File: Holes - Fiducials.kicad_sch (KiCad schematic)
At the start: 0 parts

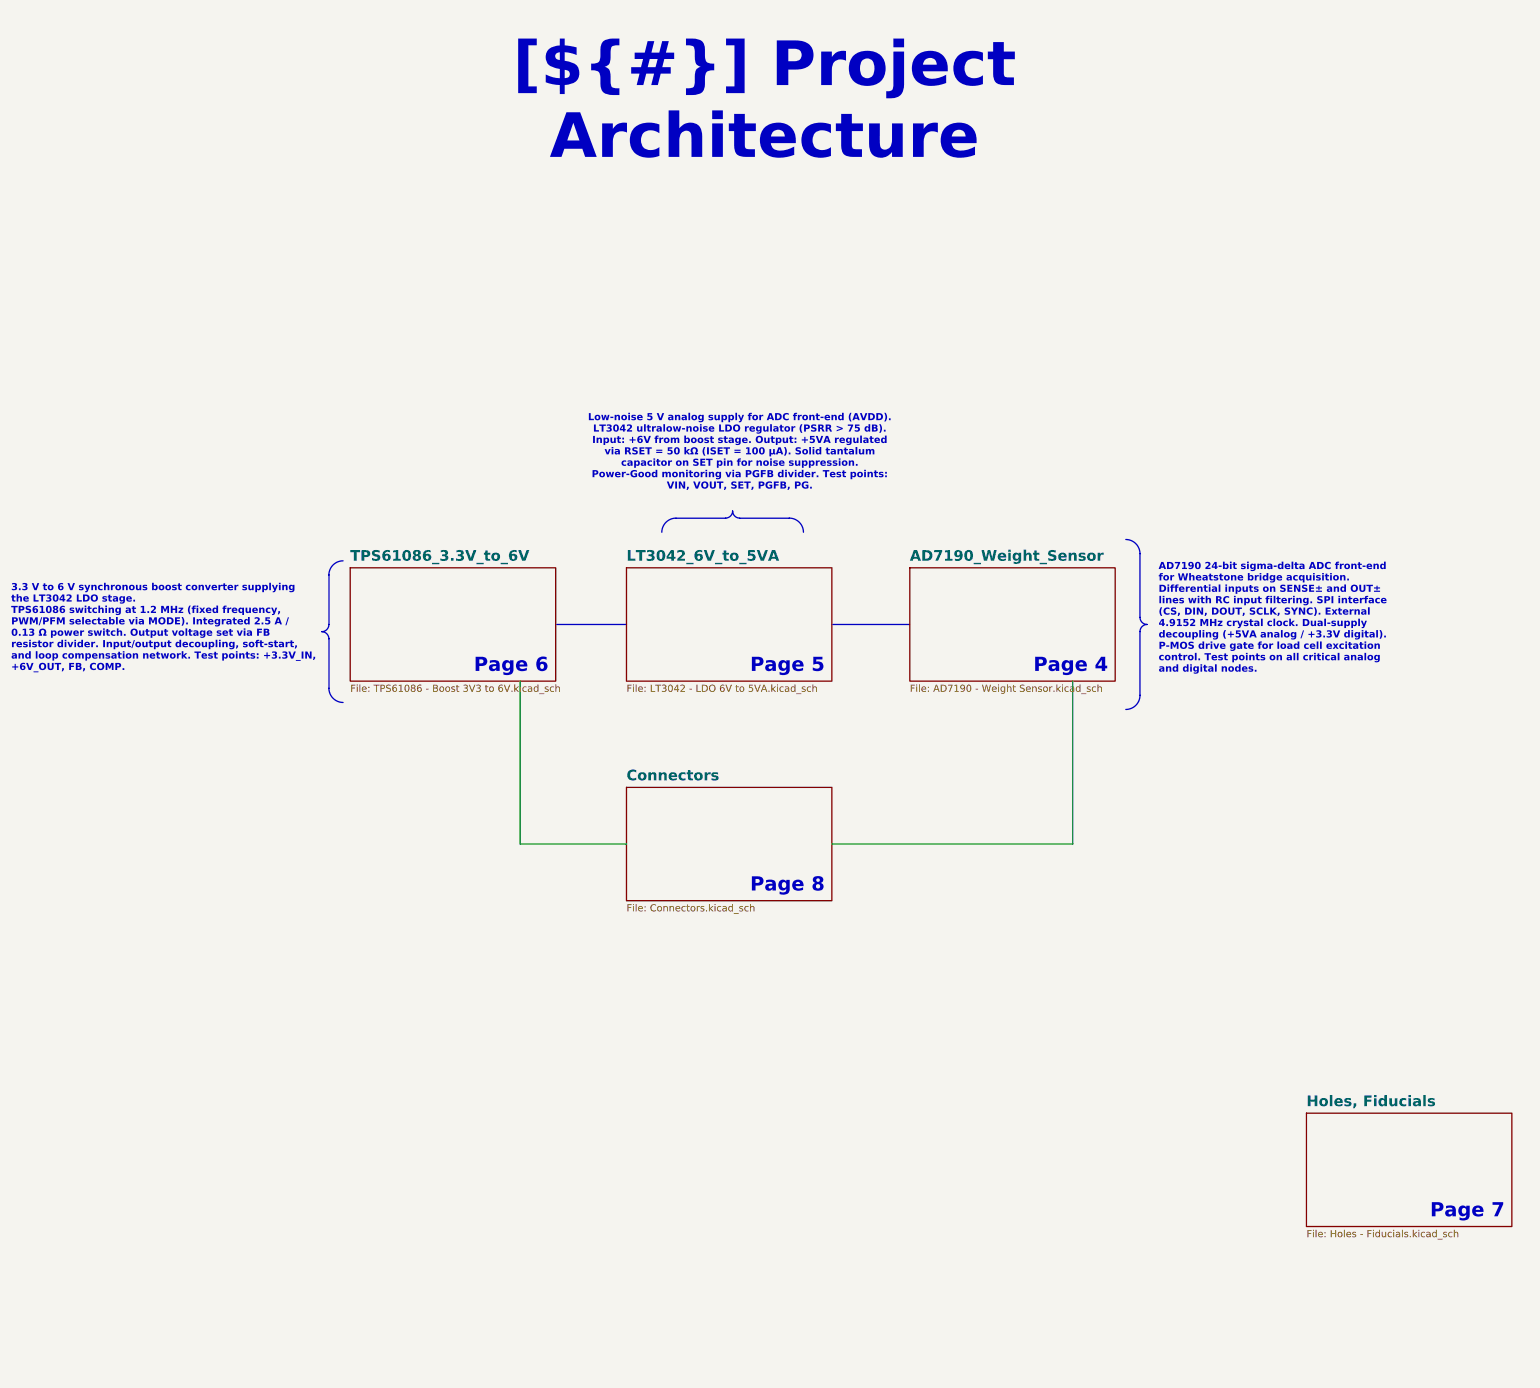
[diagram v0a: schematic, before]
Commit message: Clean up project for KDT template: rename, metadata, KiCad 10 CI
- Rename project Cellule_de_force_V2 -> OPEN_WEIGHT and sheets after their function
  (fix AD7910 -> AD7190 typo), update all sheet/project references in sch/pcb/pro
- Real title-block titles, sheet headers use ${TITLE}, restore KDT drawing sheets,
  remove template leftovers from PCB title block
- kibot_main.yaml: COMPANY = OPEN THRUST LAB, GIT_URL = foukouda/OPEN_WEIGHT
- CI: add KiCad 10 (KiBot v2_dk10), PRELIMINARY variant on dev
- README now generated from kibot_resources/templates/readme.txt; fill CHANGELOG
- Move mechanical CAD to Mechanical/, extend .gitignore, untrack 3Dx logs

Co-Authored-By: Claude Opus 5.5 <noreply@anthropic.com>
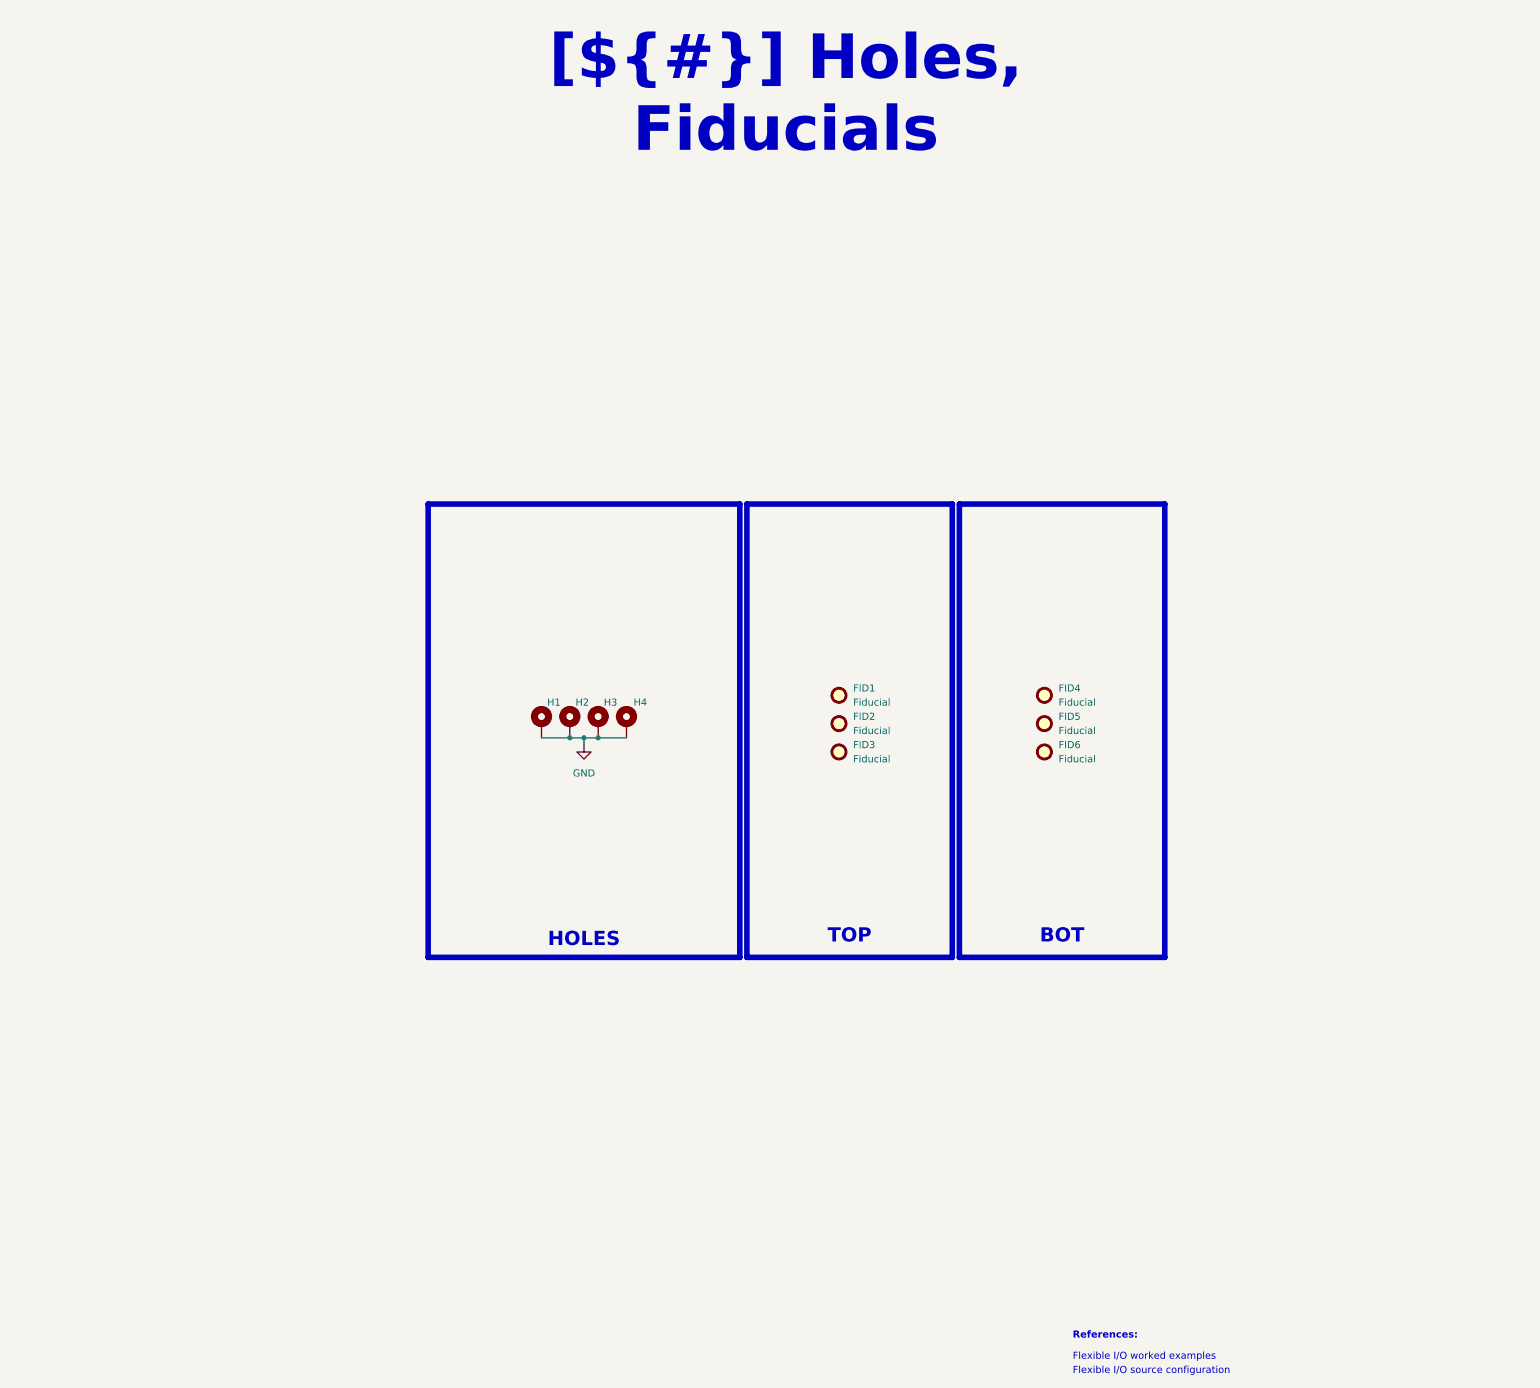
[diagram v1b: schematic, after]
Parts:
- added FID1, FID2, FID3, FID4, FID5, FID6: Fiducial, Fiducial:Fiducial_1.5mm_Mask3mm, symbol Mechanical:Fiducial
- added H1, H2, H3, H4: MountingHole_Pad, MountingHole:MountingHole_3.2mm_M3_Pad_Via, symbol Mechanical:MountingHole_Pad
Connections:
- new net GND: H1.1, H2.1, H3.1, H4.1
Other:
- removed sheet AD7190_Weight_Sensor
- removed sheet Connectors
- removed sheet Holes, Fiducials
- removed sheet LT3042_6V_to_5VA
- removed sheet TPS61086_3.3V_to_6V
- note added: "Flexible I/O source configuration"
- note added: "Flexible I/O worked examples"
- note added: "References:"
- note removed: "Page 4"
- note removed: "Page 5"
- note removed: "Page 6"
- note removed: "Page 7"
- note removed: "Page 8"
- title: Project Architecture -> Holes, Fiducials

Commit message: Self-contained libraries, JLCPCB rules, ERC/DRC cleanup
- lib/: project symbol library (19 symbols), footprint library (17 footprints)
  and all 3D models (15), referenced through ${KIPRJMOD} + project lib tables.
  A fresh clone now opens with every symbol, footprint and 3D model.
- Remove duplicated / absolute 3D model paths (C:/Users/..., ${KICAD_FOOTPRINT})
- OPEN_WEIGHT.kicad_dru: JLCPCB 4-layer rules; stackup JLC04161H-7628; board minimums
- AD7190 footprint: drop per-pad 0.102 mm mask margin (mask bridges at 0.65 mm pitch)
- Exclude unplaced TP/FID symbols from board; PWR_FLAGs; decorative wires -> lines
- Local text variables in .kicad_pro; Revision History wired to [Unreleased]
- get_changelog.py: accept "## [Unreleased]" without date
ERC: 0 errors. DRC: 0 errors except 10 courtyard overlaps (placement), 0 parity issues.

Co-Authored-By: Claude Opus 5.5 <noreply@anthropic.com>
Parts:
- FID1, FID2, FID3, FID4, FID5, FID6: symbol Mechanical:Fiducial -> OPEN_WEIGHT:Fiducial
- H1, H2, H3, H4: footprint MountingHole:MountingHole_3.2mm_M3_Pad_Via -> OPEN_WEIGHT:MountingHole_3.2mm_M3_Pad_Via; symbol Mechanical:MountingHole_Pad -> OPEN_WEIGHT:MountingHole_Pad
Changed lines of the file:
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@@
 	)
 	(symbol
-		(lib_id "Mechanical:Fiducial")
+		(lib_id "OPEN_WEIGHT:Fiducial")
 		(at 223.52 139.7 0)
 		(unit 1)
@@
 		(exclude_from_sim no)
 		(in_bom no)
-		(on_board yes)
-		(in_pos_files yes)
+		(on_board no)
+		(in_pos_files no)
 		(dnp no)
 		(fields_autoplaced yes)
@@
 	)
 	(symbol
-		(lib_id "Mechanical:MountingHole_Pad")
+		(lib_id "OPEN_WEIGHT:MountingHole_Pad")
 		(at 185.42 139.7 0)
 		(unit 1)
@@
 			)
 		)
-		(property "Footprint" "MountingHole:MountingHole_3.2mm_M3_Pad_Via"
+		(property "Footprint" "OPEN_WEIGHT:MountingHole_3.2mm_M3_Pad_Via"
 			(at 185.42 139.7 0)
 			(hide yes)
@@
 	)
 	(symbol
-		(lib_id "Mechanical:MountingHole_Pad")
+		(lib_id "OPEN_WEIGHT:MountingHole_Pad")
 		(at 170.18 139.7 0)
 		(unit 1)
@@
 			)
 		)
-		(property "Footprint" "MountingHole:MountingHole_3.2mm_M3_Pad_Via"
+		(property "Footprint" "OPEN_WEIGHT:MountingHole_3.2mm_M3_Pad_Via"
 			(at 170.18 139.7 0)
 			(hide yes)
@@
 	)
 	(symbol
-		(lib_id "Mechanical:Fiducial")
+		(lib_id "OPEN_WEIGHT:Fiducial")
 		(at 223.52 144.78 0)
 		(unit 1)
@@
 		(exclude_from_sim no)
 		(in_bom no)
-		(on_board yes)
-		(in_pos_files yes)
+		(on_board no)
+		(in_pos_files no)
 		(dnp no)
 		(fields_autoplaced yes)
@@
 	)
 	(symbol
-		(lib_id "Mechanical:MountingHole_Pad")
+		(lib_id "OPEN_WEIGHT:MountingHole_Pad")
 		(at 175.26 139.7 0)
 		(unit 1)
@@
 			)
 		)
-		(property "Footprint" "MountingHole:MountingHole_3.2mm_M3_Pad_Via"
+		(property "Footprint" "OPEN_WEIGHT:MountingHole_3.2mm_M3_Pad_Via"
 			(at 175.26 139.7 0)
 			(hide yes)
@@
 	)
 	(symbol
-		(lib_id "Mechanical:Fiducial")
+		(lib_id "OPEN_WEIGHT:Fiducial")
 		(at 260.35 134.62 0)
 		(unit 1)
@@
 		(exclude_from_sim no)
 		(in_bom no)
-		(on_board yes)
-		(in_pos_files yes)
+		(on_board no)
+		(in_pos_files no)
 		(dnp no)
 		(fields_autoplaced yes)
@@
 	)
 	(symbol
-		(lib_id "Mechanical:Fiducial")
+		(lib_id "OPEN_WEIGHT:Fiducial")
 		(at 260.35 144.78 0)
 		(unit 1)
@@
 		(exclude_from_sim no)
 		(in_bom no)
-		(on_board yes)
-		(in_pos_files yes)
+		(on_board no)
+		(in_pos_files no)
 		(dnp no)
 		(fields_autoplaced yes)
@@
 	)
 	(symbol
-		(lib_id "Mechanical:MountingHole_Pad")
+		(lib_id "OPEN_WEIGHT:MountingHole_Pad")
 		(at 180.34 139.7 0)
 		(unit 1)
@@
 			)
 		)
-		(property "Footprint" "MountingHole:MountingHole_3.2mm_M3_Pad_Via"
+		(property "Footprint" "OPEN_WEIGHT:MountingHole_3.2mm_M3_Pad_Via"
 			(at 180.34 139.7 0)
 			(hide yes)
@@
 	)
 	(symbol
-		(lib_id "Mechanical:Fiducial")
+		(lib_id "OPEN_WEIGHT:Fiducial")
 		(at 260.35 139.7 0)
 		(unit 1)
@@
 		(exclude_from_sim no)
 		(in_bom no)
-		(on_board yes)
-		(in_pos_files yes)
+		(on_board no)
+		(in_pos_files no)
 		(dnp no)
 		(fields_autoplaced yes)
@@
 	)
 	(symbol
-		(lib_id "Mechanical:Fiducial")
+		(lib_id "OPEN_WEIGHT:Fiducial")
 		(at 223.52 134.62 0)
 		(unit 1)
@@
 		(exclude_from_sim no)
 		(in_bom no)
-		(on_board yes)
-		(in_pos_files yes)
+		(on_board no)
+		(in_pos_files no)
 		(dnp no)
 		(fields_autoplaced yes)

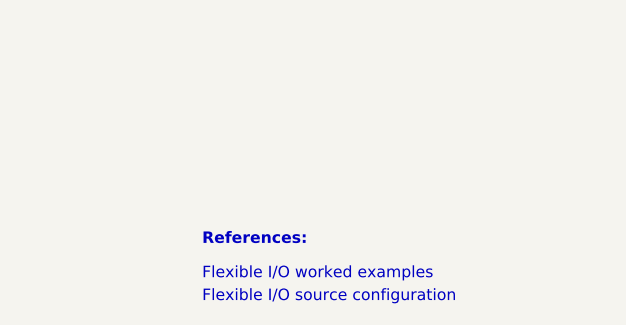
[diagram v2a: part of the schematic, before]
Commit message: Fill template pages: block diagram, power sequencing, notes, revision history
Block Diagram and Power - Sequencing rebuilt from the real design (values computed
from the schematic); cover-page design notes, connector pinout notes, title-block
references; kicad-mcp-pro MCP config (.mcp.json).

Co-Authored-By: Claude Opus 5.5 <noreply@anthropic.com>
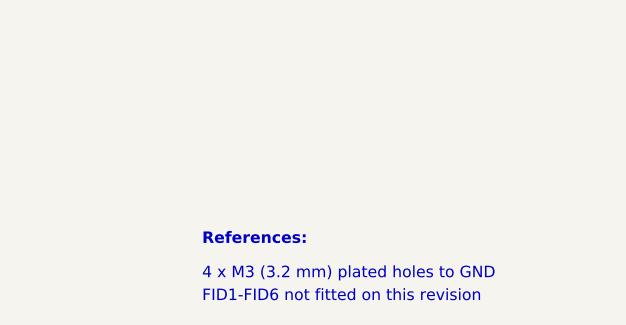
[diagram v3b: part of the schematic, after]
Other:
- note added: "4 x M3 (3.2 mm) plated holes to GND"
- note added: "FID1-FID6 not fitted on this revision"
- note removed: "Flexible I/O source configuration"
- note removed: "Flexible I/O worked examples"
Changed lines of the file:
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@@
 		)
 	)
-	(text "Flexible I/O worked examples"
+	(text "4 x M3 (3.2 mm) plated holes to GND"
 		(exclude_from_sim no)
 		(at 265.43 254 0)
@@
 		)
 	)
-	(text "Flexible I/O source configuration"
+	(text "FID1-FID6 not fitted on this revision"
 		(exclude_from_sim no)
 		(at 265.43 256.54 0)
